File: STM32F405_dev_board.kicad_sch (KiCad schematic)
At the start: 42 parts, among them IC2 FT232RNL-REEL, J1 Conn_ARM_JTAG_SWD_20, J2 Conn_01x20_Pin, J3 Conn_01x20_Pin, J6 USB4800-03-A, U1 STM32F405RGT6, Y1 8MHz, Y2 Crystal_GND23

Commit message: Changed 8MHz oscillator to SMD one
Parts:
- Y1: footprint Crystal:Crystal_HC49-4H_Vertical -> Crystal:Crystal_SMD_HC49-SD_HandSoldering
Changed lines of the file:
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@@
       (effects (font (size 1.27 1.27)) (justify right))
     )
-    (property "Footprint" "Crystal:Crystal_HC49-4H_Vertical" (at 255.27 31.75 0)
+    (property "Footprint" "Crystal:Crystal_SMD_HC49-SD_HandSoldering" (at 255.27 31.75 0)
       (effects (font (size 1.27 1.27)) hide)
     )

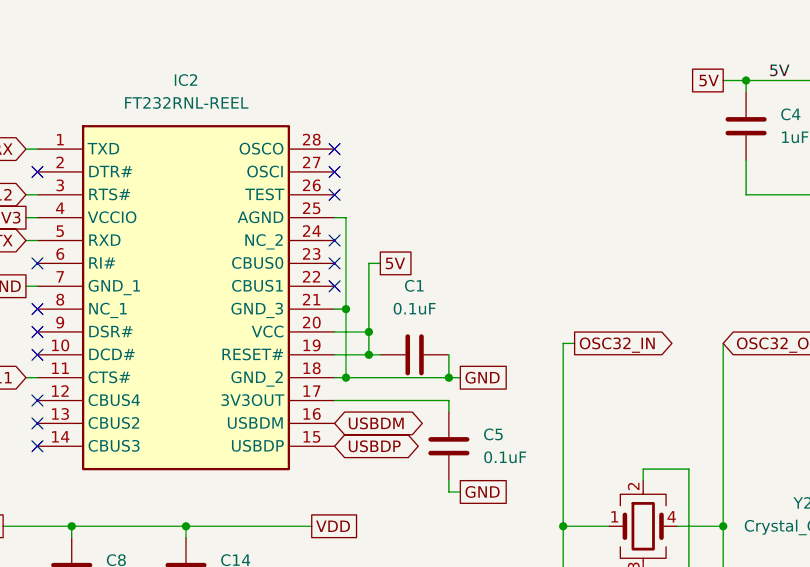
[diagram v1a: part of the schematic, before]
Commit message: Fixed FT232RL connection
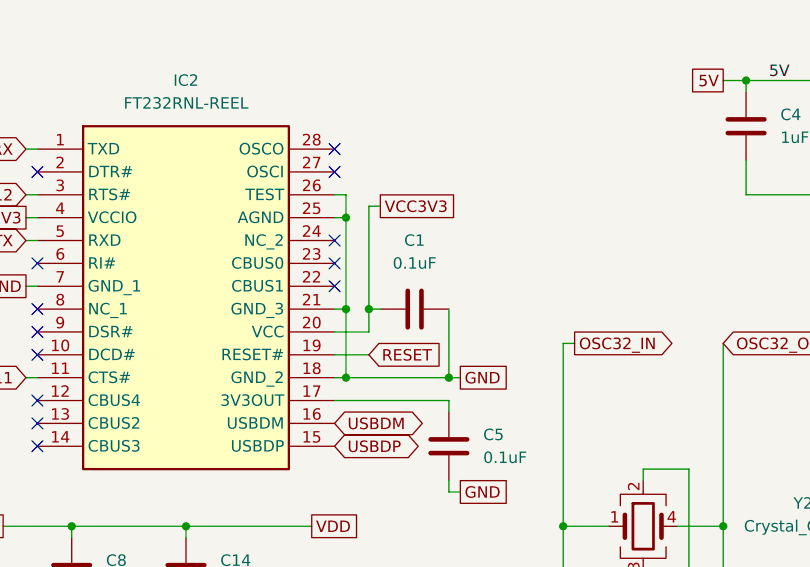
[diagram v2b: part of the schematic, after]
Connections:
- net 5V: no longer C1.2, IC2.19 (RESET#), IC2.20 (VCC)
- net GND: now also IC2.26 (TEST)
- net RESET: now also IC2.19 (RESET#)
- net VCC3V3: now also C1.2, IC2.20 (VCC)
- no-connect marks 16 -> 15
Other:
- moved on the sheet: C1
